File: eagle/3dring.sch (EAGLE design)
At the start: 12 parts, among them U1 Tiny45-20-SMT, U2 NCP1402

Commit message: board file added and ordered
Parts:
- removed C1: 10uF, SparkFun:CAP_POL1206
- removed C2: 68uF, SparkFun:CAP_POL3528
- removed C3, C4: 100nf, SparkFun-Passives:CAP0603-CAP
- removed D1: MBRA140, SparkFun:DIODESMA
- removed D2: GREEN, SparkFun-LED:LED-GREEN0603
- removed JP1: (no value), SparkFun:M03PTH
- removed L1: 47uH, SparkFun:INDUCTORCR54
- removed U2: NCP1402, SparkFun:V_REG_NCP1400SOT23-5
- added C5, C6, C8: 0.1uF, SparkFun:CAP0402-CAP
- added C7, C9: 100nF, rcl:C-EUC0402
- added CN2: M02JST-PTH-2, SparkFun-Connectors:M02JST-PTH-2
- added IC7: TLV71333DBV, anoven:TLV71333DBV
- added IR: (no value), SparkFun-LED:LED5MM
- added JP3: (no value), SparkFun-Connectors:M06SMD-1MM
- added LED1: BLUE, SparkFun:LED0603
- added R2: 1k, SparkFun:RESISTOR0402-RES
- added R3: 10k, SparkFun:RESISTOR0402-RES
- added R4, R5: 1M, SparkFun:RESISTOR0402-RES
- added U3: ATMEGA328, SparkFun:ATMEGA168
- added Y1: 8Mhz, murata-filter:CSTCR6M00G53Z
- R1: value 1k -> 330; device SparkFun-Passives:RESISTOR0603-RES -> SparkFun:RESISTOR0402-RES
- U1: value Tiny45-20-SMT -> WS2811; device SparkFun-DigitalIC:ATTINY45TINY45-20-SMT -> SparkFun-LED:LED-TRICOLOR-5050-ICWS2811
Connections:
- removed net MISO: R1.2, U1.PB1(MISO)
- removed net PB3: U1.PB3(ADC3)
- removed net VIN: C1.+, JP1.3, L1.1
- removed net VOUT: JP1.2
- new net AD3: U3.PC3(ADC3)
- new net AIN2: U3.PB0(ICP)
- new net AREF: C5.1, U3.AREF
- new net B1BUTTON: R4.2, U3.PB2(SS/OC1B)
- new net B1SEND: R4.1, U3.PB1(OC1A)
- new net B2BUTTON: R5.2, U3.PB4(MISO)
- new net B2SEND: R5.1, U3.PB3(MOSI/OC2)
- new net CTS: JP3.5
- new net DTR: C8.1, JP3.1
- new net IO7: U3.PD7(AIN1)
- new net IRLED: IR.A, U3.PD5(T1)
- new net IRPWR: JP2.3, U3.PD4(XCK/T0)
- new net N$1: LED1.A, R2.2
- new net N$4: U3.PB6(XTAL1/TOSC1), Y1.1
- new net N$5: U3.PB7(XTAL2/TOSC2), Y1.3
- new net N$6: U3.ADC7
- new net POTD: U3.PC2(ADC2)
- new net POTI: U3.PC1(ADC1)
- new net POTP: U3.PC0(ADC0)
- new net PWMA: U3.PD6(AIN0)
- new net RX-I: JP3.2, U3.PD0(RXD)
- new net SCK: R2.1, U3.PB5(SCK)
- new net TX-O: JP3.3, U3.PD1(TXD)
- new net V_BATT: C7.1, CN2.2, IC7.EN, IC7.IN
- new net WS2812: U1.DI, U3.PD2(INT0)
- net GND: now also C5.2, C6.1, C7.2, C9.2, CN2.1, IC7.GND, JP3.6, LED1.C, R1.1, U1.VSS, U3.AGND, U3.GND@1, U3.GND@2, Y1.2; no longer C1.-, C2.-, C3.2, C4.2, D2.C, JP1.1, U1.GND, U2.GND
- net IRDETECT: now also U3.PD3(INT1); no longer U1.PB4(ADC2)
- net N$2: now also U3.ADC6; no longer D2.A, R1.1
- net N$3: now also IR.C, R1.2; no longer D1.A, L1.2, U2.LX
- net RESET: now also C8.2, R3.1, U3.PC6(/RESET); no longer U1.PB5(NRES)
- net SCL: now also U3.PC5(ADC5/SCL); no longer U1.PB2(SCK/ADC1)
- net SDA: now also U3.PC4(ADC4/SDA); no longer U1.PB0(MOSI)
- net VCC: now also C6.2, C9.1, IC7.OUT, JP3.4, R3.2, U1.VDD, U3.AVCC, U3.VCC@1, U3.VCC@2; no longer C2.+, C3.1, D1.C, JP2.3, U1.VCC, U2.EN, U2.OUT
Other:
- note added: "ATmega328"
- moved on the sheet: JP2, R1

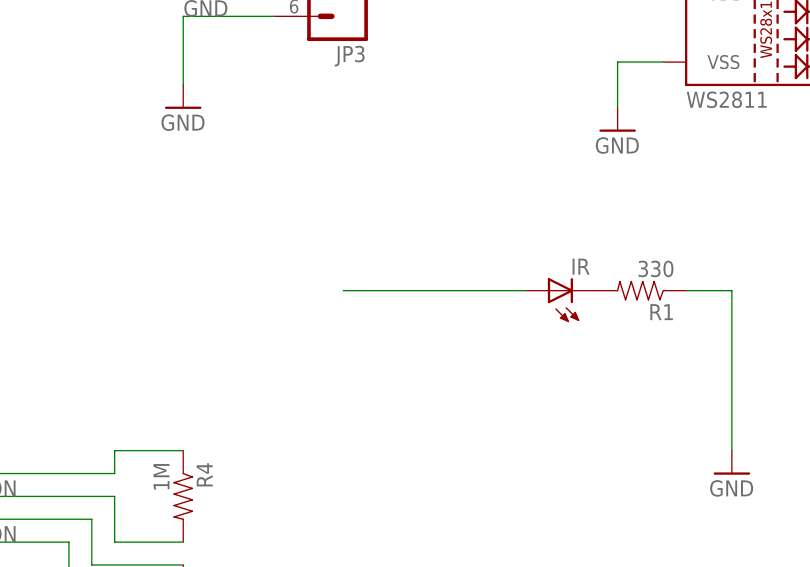
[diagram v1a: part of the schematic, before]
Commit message: Updated board problems
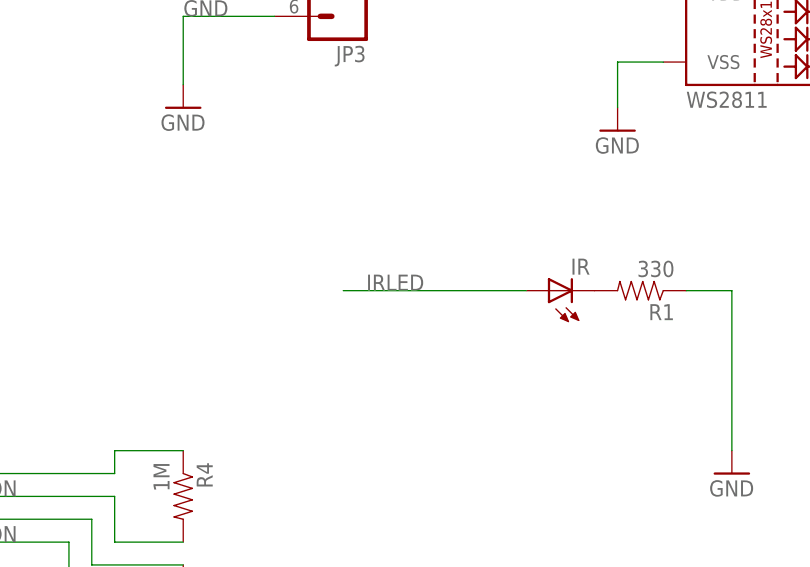
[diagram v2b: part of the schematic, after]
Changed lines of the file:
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@@
 <pinref part="IR" gate="G$1" pin="A"/>
 <wire x1="226.06" y1="48.26" x2="205.74" y2="48.26" width="0.1524" layer="91"/>
+<label x="208.28" y="48.26" size="1.778" layer="95"/>
 </segment>
 </net>

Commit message: New version
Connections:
- net IRDETECT: now also U3.PD5(T1); no longer U3.PD3(INT1)
- net IRLED: now also U3.PD3(INT1); no longer U3.PD5(T1)
- net RX-I: now also JP3.3; no longer JP3.2
- net TX-O: now also JP3.2; no longer JP3.3
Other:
- moved on the sheet: CN2, IR, JP2, JP3, R1, U1
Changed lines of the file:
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@@
 </plain>
 <instances>
-<instance part="JP2" gate="G$1" x="241.3" y="114.3" rot="R180"/>
-<instance part="GND1" gate="1" x="223.52" y="96.52"/>
+<instance part="JP2" gate="G$1" x="231.14" y="104.14" rot="R180"/>
+<instance part="GND1" gate="1" x="213.36" y="86.36"/>
 <instance part="C5" gate="G$1" x="76.2" y="53.34" smashed="yes">
 <attribute name="NAME" x="77.724" y="56.261" size="1.778" layer="95"/>
@@
 <instance part="P+8" gate="1" x="99.06" y="83.82"/>
 <instance part="P+7" gate="1" x="88.9" y="30.48"/>
-<instance part="GND15" gate="1" x="187.96" y="68.58"/>
-<instance part="JP3" gate="G$1" x="203.2" y="86.36" rot="R180"/>
-<instance part="IR" gate="G$1" x="228.6" y="48.26" rot="R90"/>
-<instance part="R1" gate="G$1" x="238.76" y="48.26" rot="R180"/>
-<instance part="GND2" gate="1" x="248.92" y="27.94"/>
-<instance part="CN2" gate="G$1" x="-22.86" y="86.36"/>
-<instance part="U$2" gate="GND" x="-7.62" y="71.12"/>
-<instance part="U1" gate="U1" x="256.54" y="76.2"/>
-<instance part="GND3" gate="1" x="236.22" y="66.04"/>
-<instance part="P+3" gate="1" x="236.22" y="88.9"/>
+<instance part="GND15" gate="1" x="177.8" y="58.42"/>
+<instance part="JP3" gate="G$1" x="193.04" y="76.2" rot="R180"/>
+<instance part="IR" gate="G$1" x="218.44" y="38.1" rot="R90"/>
+<instance part="R1" gate="G$1" x="228.6" y="38.1" rot="R180"/>
+<instance part="GND2" gate="1" x="238.76" y="17.78"/>
+<instance part="CN2" gate="G$1" x="7.62" y="83.82"/>
+<instance part="U$2" gate="GND" x="22.86" y="68.58"/>
+<instance part="U1" gate="U1" x="246.38" y="66.04"/>
+<instance part="GND3" gate="1" x="226.06" y="55.88"/>
+<instance part="P+3" gate="1" x="226.06" y="78.74"/>
 <instance part="R4" gate="G$1" x="187.96" y="25.4" rot="R270"/>
 <instance part="R5" gate="G$1" x="187.96" y="12.7" rot="R270"/>
@@
 </segment>
 <segment>
-<wire x1="198.12" y1="83.82" x2="187.96" y2="83.82" width="0.1524" layer="91"/>
-<label x="187.96" y="83.82" size="1.778" layer="95"/>
+<wire x1="187.96" y1="73.66" x2="177.8" y2="73.66" width="0.1524" layer="91"/>
+<label x="177.8" y="73.66" size="1.778" layer="95"/>
 <pinref part="JP3" gate="G$1" pin="4"/>
 </segment>
 <segment>
 <pinref part="U1" gate="U1" pin="VDD"/>
-<wire x1="241.3" y1="81.28" x2="236.22" y2="81.28" width="0.1524" layer="91"/>
-<wire x1="236.22" y1="81.28" x2="236.22" y2="88.9" width="0.1524" layer="91"/>
+<wire x1="231.14" y1="71.12" x2="226.06" y2="71.12" width="0.1524" layer="91"/>
+<wire x1="226.06" y1="71.12" x2="226.06" y2="78.74" width="0.1524" layer="91"/>
 <pinref part="P+3" gate="1" pin="VCC"/>
 </segment>
@@
 <segment>
 <pinref part="JP2" gate="G$1" pin="2"/>
-<wire x1="233.68" y1="114.3" x2="223.52" y2="114.3" width="0.1524" layer="91"/>
-<wire x1="223.52" y1="114.3" x2="223.52" y2="99.06" width="0.1524" layer="91"/>
+<wire x1="223.52" y1="104.14" x2="213.36" y2="104.14" width="0.1524" layer="91"/>
+<wire x1="213.36" y1="104.14" x2="213.36" y2="88.9" width="0.1524" layer="91"/>
 <pinref part="GND1" gate="1" pin="GND"/>
 </segment>
@@
 </segment>
 <segment>
-<wire x1="198.12" y1="78.74" x2="187.96" y2="78.74" width="0.1524" layer="91"/>
-<wire x1="187.96" y1="78.74" x2="187.96" y2="71.12" width="0.1524" layer="91"/>
+<wire x1="187.96" y1="68.58" x2="177.8" y2="68.58" width="0.1524" layer="91"/>
+<wire x1="177.8" y1="68.58" x2="177.8" y2="60.96" width="0.1524" layer="91"/>
 <pinref part="GND15" gate="1" pin="GND"/>
-<label x="187.96" y="78.74" size="1.778" layer="95"/>
+<label x="177.8" y="68.58" size="1.778" layer="95"/>
 <pinref part="JP3" gate="G$1" pin="6"/>
 </segment>
 <segment>
-<wire x1="248.92" y1="48.26" x2="248.92" y2="30.48" width="0.1524" layer="91"/>
+<wire x1="238.76" y1="38.1" x2="238.76" y2="20.32" width="0.1524" layer="91"/>
 <pinref part="GND2" gate="1" pin="GND"/>
 <pinref part="R1" gate="G$1" pin="1"/>
-<wire x1="243.84" y1="48.26" x2="248.92" y2="48.26" width="0.1524" layer="91"/>
+<wire x1="233.68" y1="38.1" x2="238.76" y2="38.1" width="0.1524" layer="91"/>
 </segment>
 <segment>
 <pinref part="CN2" gate="G$1" pin="1"/>
-<wire x1="-15.24" y1="86.36" x2="-7.62" y2="86.36" width="0.1524" layer="91"/>
-<wire x1="-7.62" y1="86.36" x2="-7.62" y2="73.66" width="0.1524" layer="91"/>
+<wire x1="15.24" y1="83.82" x2="22.86" y2="83.82" width="0.1524" layer="91"/>
+<wire x1="22.86" y1="83.82" x2="22.86" y2="71.12" width="0.1524" layer="91"/>
 <pinref part="U$2" gate="GND" pin="GND"/>
 </segment>
@@
 <pinref part="U1" gate="U1" pin="VSS"/>
 <pinref part="GND3" gate="1" pin="GND"/>
-<wire x1="241.3" y1="73.66" x2="236.22" y2="73.66" width="0.1524" layer="91"/>
-<wire x1="236.22" y1="73.66" x2="236.22" y2="68.58" width="0.1524" layer="91"/>
+<wire x1="231.14" y1="63.5" x2="226.06" y2="63.5" width="0.1524" layer="91"/>
+<wire x1="226.06" y1="63.5" x2="226.06" y2="58.42" width="0.1524" layer="91"/>
 </segment>
 </net>
@@
 <segment>
 <pinref part="JP2" gate="G$1" pin="1"/>
-<wire x1="233.68" y1="116.84" x2="223.52" y2="116.84" width="0.1524" layer="91"/>
-<label x="215.9" y="116.84" size="1.778" layer="95"/>
-</segment>
-<segment>
-<pinref part="U3" gate="G$1" pin="PD3(INT1)"/>
-<wire x1="149.86" y1="45.72" x2="162.56" y2="45.72" width="0.1524" layer="91"/>
-<label x="154.94" y="45.72" size="1.778" layer="95"/>
+<wire x1="223.52" y1="106.68" x2="213.36" y2="106.68" width="0.1524" layer="91"/>
+<label x="205.74" y="106.68" size="1.778" layer="95"/>
+</segment>
+<segment>
+<wire x1="162.56" y1="40.64" x2="149.86" y2="40.64" width="0.1524" layer="91"/>
+<label x="157.48" y="40.64" size="1.778" layer="95"/>
+<pinref part="U3" gate="G$1" pin="PD5(T1)"/>
 </segment>
 </net>
@@
 </segment>
 <segment>
-<wire x1="198.12" y1="91.44" x2="187.96" y2="91.44" width="0.1524" layer="91"/>
-<label x="187.96" y="91.44" size="1.778" layer="95"/>
+<wire x1="187.96" y1="81.28" x2="177.8" y2="81.28" width="0.1524" layer="91"/>
+<label x="177.8" y="81.28" size="1.778" layer="95"/>
 <pinref part="JP3" gate="G$1" pin="1"/>
 </segment>
@@
 </segment>
 <segment>
-<wire x1="198.12" y1="88.9" x2="187.96" y2="88.9" width="0.1524" layer="91"/>
-<label x="187.96" y="88.9" size="1.778" layer="95"/>
-<pinref part="JP3" gate="G$1" pin="2"/>
+<wire x1="187.96" y1="76.2" x2="177.8" y2="76.2" width="0.1524" layer="91"/>
+<label x="177.8" y="76.2" size="1.778" layer="95"/>
+<pinref part="JP3" gate="G$1" pin="3"/>
 </segment>
 </net>
@@
 </segment>
 <segment>
-<wire x1="198.12" y1="86.36" x2="187.96" y2="86.36" width="0.1524" layer="91"/>
-<label x="187.96" y="86.36" size="1.778" layer="95"/>
-<pinref part="JP3" gate="G$1" pin="3"/>
+<wire x1="187.96" y1="78.74" x2="177.8" y2="78.74" width="0.1524" layer="91"/>
+<label x="177.8" y="78.74" size="1.778" layer="95"/>
+<pinref part="JP3" gate="G$1" pin="2"/>
 </segment>
 </net>
@@
 <segment>
 <pinref part="JP2" gate="G$1" pin="3"/>
-<wire x1="233.68" y1="111.76" x2="228.6" y2="111.76" width="0.1524" layer="91"/>
+<wire x1="223.52" y1="101.6" x2="218.44" y2="101.6" width="0.1524" layer="91"/>
 </segment>
 </net>
@@
 <net name="CTS" class="0">
 <segment>
-<wire x1="200.66" y1="81.28" x2="198.12" y2="81.28" width="0.1524" layer="91"/>
-<label x="187.96" y="81.28" size="1.778" layer="95"/>
+<wire x1="190.5" y1="71.12" x2="187.96" y2="71.12" width="0.1524" layer="91"/>
+<label x="177.8" y="71.12" size="1.778" layer="95"/>
 <pinref part="JP3" gate="G$1" pin="5"/>
-<wire x1="198.12" y1="81.28" x2="187.96" y2="81.28" width="0.1524" layer="91"/>
-<junction x="198.12" y="81.28"/>
+<wire x1="187.96" y1="71.12" x2="177.8" y2="71.12" width="0.1524" layer="91"/>
+<junction x="187.96" y="71.12"/>
 </segment>
 </net>
@@
 <segment>
 <pinref part="CN2" gate="G$1" pin="2"/>
-<wire x1="-15.24" y1="88.9" x2="-7.62" y2="88.9" width="0.1524" layer="91"/>
-<label x="-12.7" y="88.9" size="1.778" layer="95"/>
+<wire x1="15.24" y1="86.36" x2="22.86" y2="86.36" width="0.1524" layer="91"/>
+<label x="17.78" y="86.36" size="1.778" layer="95"/>
 </segment>
 </net>
 <net name="IRLED" class="0">
 <segment>
-<wire x1="162.56" y1="40.64" x2="149.86" y2="40.64" width="0.1524" layer="91"/>
-<label x="157.48" y="40.64" size="1.778" layer="95"/>
-<pinref part="U3" gate="G$1" pin="PD5(T1)"/>
-</segment>
-<segment>
 <pinref part="IR" gate="G$1" pin="A"/>
-<wire x1="226.06" y1="48.26" x2="205.74" y2="48.26" width="0.1524" layer="91"/>
-<label x="208.28" y="48.26" size="1.778" layer="95"/>
+<wire x1="215.9" y1="38.1" x2="195.58" y2="38.1" width="0.1524" layer="91"/>
+<label x="198.12" y="38.1" size="1.778" layer="95"/>
+</segment>
+<segment>
+<pinref part="U3" gate="G$1" pin="PD3(INT1)"/>
+<wire x1="149.86" y1="45.72" x2="162.56" y2="45.72" width="0.1524" layer="91"/>
+<label x="154.94" y="45.72" size="1.778" layer="95"/>
 </segment>
 </net>
@@
 <segment>
 <pinref part="U1" gate="U1" pin="DI"/>
-<wire x1="269.24" y1="81.28" x2="279.4" y2="81.28" width="0.1524" layer="91"/>
-<label x="274.32" y="81.28" size="1.778" layer="95"/>
-</segment>
-<segment>
+<wire x1="259.08" y1="71.12" x2="269.24" y2="71.12" width="0.1524" layer="91"/>
+<label x="264.16" y="71.12" size="1.778" layer="95"/>
+</segment>
+<segment>
